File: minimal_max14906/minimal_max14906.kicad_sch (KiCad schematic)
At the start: 75 parts, among them J1 CLP-114-02-G-D-BE, J2 CLP-102-02-G-D-BE, J3 CLP-102-02-G-D-BE, J4 CLP-102-02-G-D-BE, J5 CLP-102-02-G-D-BE, J6 CLP-102-02-G-D-BE, J7 CLP-102-02-G-D-BE, Q1 SI7309DN-T1-E3, Q2 SI7309DN-T1-E3, Q3 SI7309DN-T1-E3, Q4 SI7309DN-T1-E3, U1 MAX14906ATM+

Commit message: Backup
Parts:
- added D10, D11, D12, D13: 40 V, diode_footprints:DO-214AB-2, symbol UNITED_DIODES_DATA_BASE:D_SMCJ40A-CA
- added J10, J11, J8, J9: TBP02R2-381-02BE, connector_footprints:TBP02R2-381-02BE, symbol UNITED_CONNECTORS_DATA_BASE:J_TBP02R2-381-02BE
- C1, C10, C12, C3, C4, C9: value 1 uF -> 1 µF; 3dviewer Link (none) -> https://3dviewer.net/index.html#model=https://github.com/io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; Capacitor Type (none) -> Ceramic
- C11, C2: value 0.1uF -> 100 nF; 3dviewer Link (none) -> https://3dviewer.net/index.html#model=https://github.com/io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; Capacitor Type (none) -> Ceramic
- C13: value 10 uF -> 10 µF; 3dviewer Link (none) -> https://3dviewer.net/index.html#model=https://github.com/io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; Capacitor Type (none) -> Ceramic
- C5, C6, C7, C8: 3dviewer Link (none) -> https://3dviewer.net/index.html#model=https://github.com/io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; Capacitor Type (none) -> Ceramic
- D1, D2, D4, D6, D8: value APHHS1005CGCK -> 1.8 V
- D3, D5, D7, D9: value APHHS1005LSECK/J3-PF -> 1.8 V
- J1, J2, J3, J4, J5, J6, J7: Mounting Style Through Hole -> Surface Mount
- Q1, Q2, Q3, Q4: value SI7309DN-T1-E3 -> -60.0 V; 3dviewer Link (none) -> https://3dviewer.net/index.html#model=https://github.com/io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
- R1: value 24.9k -> 24.9 kΩ; 3dviewer Link (none) -> https://3dviewer.net/index.html#model=https://github.com/io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; Component Type (none) -> Resistor
- R2, R3, R4, R5: value 5.6k -> 5.6 kΩ; 3dviewer Link (none) -> https://3dviewer.net/index.html#model=https://github.com/io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; Component Type (none) -> Resistor
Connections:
- net CHANNEL_1: now also D12.1, J10.2
- net CHANNEL_2: now also D13.1, J11.1
- net CHANNEL_3: now also D11.1, J9.2
- net CHANNEL_4: now also D10.1, J8.1
- net GNDA: now also D10.2, D11.2, D12.2, D13.2, J10.1, J11.2, J8.2, J9.1
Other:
- moved on the sheet: J4, TP15, TP16, TP17, TP18, TP20, TP21, TP22, TP23, TP24, TP25, TP26

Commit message: Switch to KiCad 9
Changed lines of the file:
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@@
 (kicad_sch
-	(version 20231120)
+	(version 20250114)
 	(generator "eeschema")
-	(generator_version "8.0")
+	(generator_version "9.0")
 	(paper "A3")
 	(junction
@@
 		)
 	)
+	(embedded_fonts no)
 )

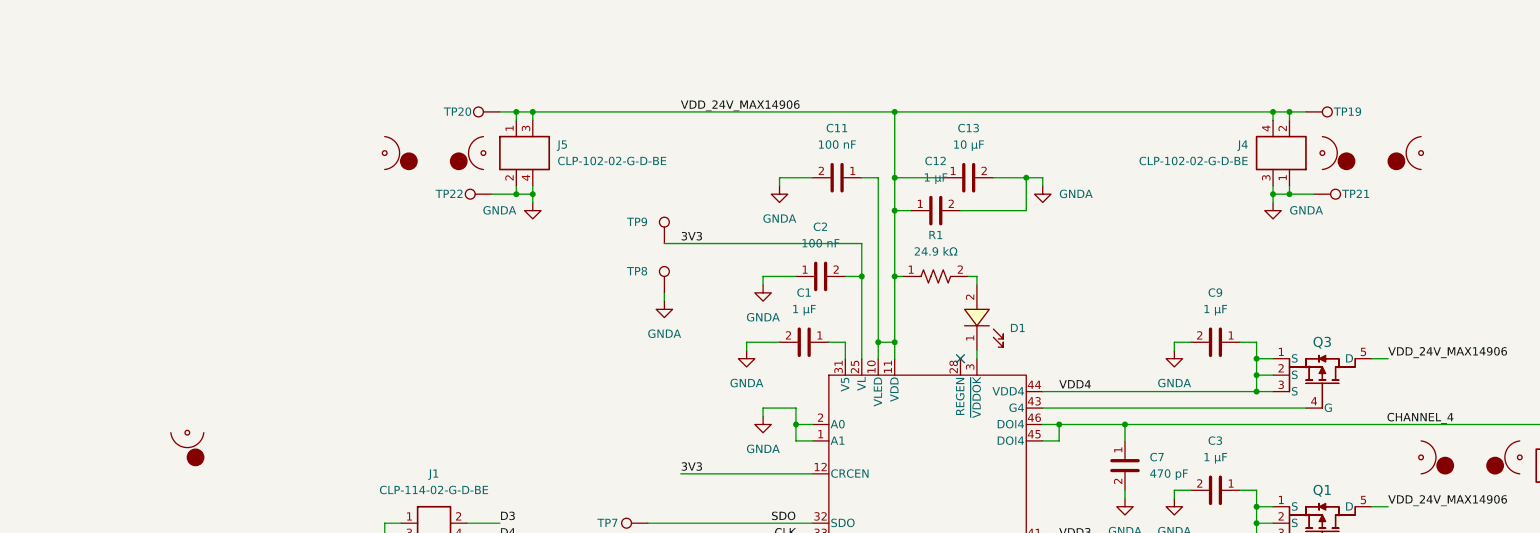
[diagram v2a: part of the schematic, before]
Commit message: Update pad dimensions and add net colors for minimal_max14906
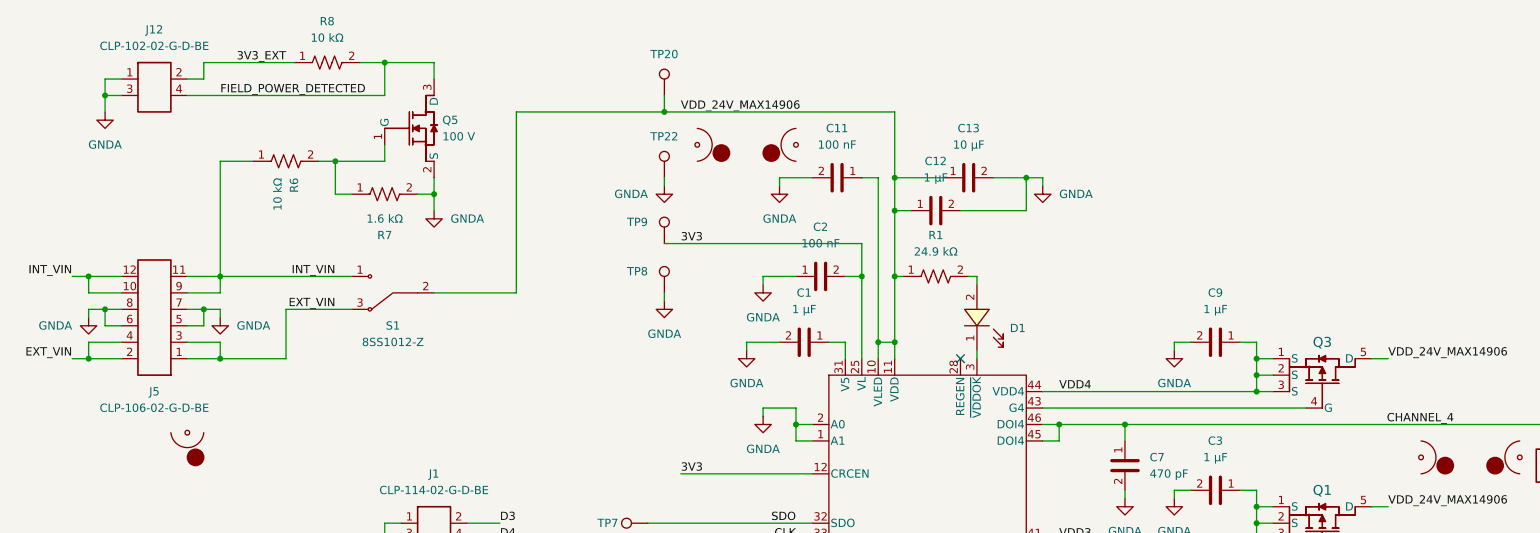
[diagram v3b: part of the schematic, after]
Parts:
- removed J4: CLP-102-02-G-D-BE, connector_footprints:CLP-102-02-G-D-BE, symbol UNITED_CONNECTORS_DATA_BASE:J_CLP-102-02-G-D-BE
- removed MB4: mouse-bite-midle-50mil-200mil, mouse_bite_footprints:mouse-bite-midle-50mil-200mil, symbol UNITED_MOUSE_BITES_DATA_BASE:mouse-bite-midle-50mil-200mil
- removed TP19, TP21: TestPoint, test_point_footprints:TestPoint_THTPad_Castelated, symbol UNITED_TEST_POINTS:TestPoint_Castelated
- added J12: CLP-102-02-G-D-BE, connector_footprints:CLP-102-02-G-D-BE, symbol UNITED_CONNECTORS_DATA_BASE:J_CLP-102-02-G-D-BE
- added Q5: 100 V, transistor_footprints:SOT-323, symbol UNITED_TRANSISTORS_DATA_BASE:Q_BSS123WQ-7-F
- added R6, R8: 10 kΩ, resistor_footprints:R_0402_1005Metric, symbol UNITED_RESISTORS_DATA_BASE:R_ERJ-2RKF1002X
- added R7: 1.6 kΩ, resistor_footprints:R_0402_1005Metric, symbol UNITED_RESISTORS_DATA_BASE:R_ERJ-2RKF1601X
- added S1: 8SS1012-Z, switches_footprints:8SS1012-Z, symbol UNITED_SWITCHES_DATA_BASE:S_8SS1012-Z
- J5: value CLP-102-02-G-D-BE -> CLP-106-02-G-D-BE; footprint connector_footprints:CLP-102-02-G-D-BE -> connector_footprints:CLP-106-02-G-D-BE; symbol UNITED_CONNECTORS_DATA_BASE:J_CLP-102-02-G-D-BE -> UNITED_CONNECTORS_DATA_BASE:J_CLP-106-02-G-D-BE; MPN CLP-102-02-G-D-BE -> CLP-106-02-G-D-BE; Pin Count 2 -> 6; Symbol Name J_CLP-102-02-G-D-BE -> J_CLP-106-02-G-D-BE; Trustedparts Search https://www.trustedparts.com/en/search/CLP-102-02-G-D-BE -> https://www.trustedparts.com/en/search/CLP-106-02-G-D-BE
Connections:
- net GNDA: now also J5.5, J5.6, J5.7, J5.8, J12.1, J12.3, Q5.2 (S), R7.2; no longer J5.2, J5.4
- net VDD_24V_MAX14906: now also S1.2; no longer J5.1, J5.3
- new net: Q5.1 (G), R6.2, R7.1
- new net 3V3_EXT: J12.2, R8.1
- new net EXT_VIN: J5.1, J5.2, J5.3, J5.4, S1.3
- new net FIELD_POWER_DETECTED: J12.4, Q5.3 (D), R8.2
- new net INT_VIN: J5.10, J5.11, J5.12, J5.9, R6.1, S1.1
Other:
- moved on the sheet: TP20, TP22

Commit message: backup
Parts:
- J5: value CLP-106-02-G-D-BE -> CLP-103-02-G-D-BE; footprint connector_footprints:CLP-106-02-G-D-BE -> connector_footprints:CLP-103-02-G-D-BE; symbol UNITED_CONNECTORS_DATA_BASE:J_CLP-106-02-G-D-BE -> UNITED_CONNECTORS_DATA_BASE:J_CLP-103-02-G-D-BE; MPN CLP-106-02-G-D-BE -> CLP-103-02-G-D-BE; Pin Count 6 -> 3; Symbol Name J_CLP-106-02-G-D-BE -> J_CLP-103-02-G-D-BE; Trustedparts Search https://www.trustedparts.com/en/search/CLP-106-02-G-D-BE -> https://www.trustedparts.com/en/search/CLP-103-02-G-D-BE
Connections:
- net EXT_VIN: now also J5.5, J5.6; no longer J5.1, J5.2, J5.3, J5.4
- net GNDA: now also J5.3, J5.4; no longer J5.5, J5.6, J5.7, J5.8
- net INT_VIN: now also J5.1, J5.2; no longer J5.10, J5.11, J5.12, J5.9

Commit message: development backup
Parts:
- added C1, C13, C14, C15, C16, C2, C3, C4: 100 nF, capacitor_footprints:C_0402_1005Metric, symbol UNITED_CAPACITORS_DATA_BASE:C_GCM155R71H104KE02D
- added C10, C11, C12, C5, C6, C7, C8, C9: 1 nF, capacitor_footprints:C_0402_1005Metric, symbol UNITED_CAPACITORS_DATA_BASE:C_GCM155R71H102KA37D
- added J6: CLP-102-02-G-D-BE, connector_footprints:CLP-102-02-G-D-BE, symbol UNITED_CONNECTORS_DATA_BASE:J_CLP-102-02-G-D-BE
- added U1, U4: ADUM1252AUA+, analog_devices_footprints:21-0036_ADI, symbol UNITED_IC_ADI:U_ADUM1252AUA+
- added U2: MAX22441CAEE+, analog_devices_footprints:21-0055_E16MS&plus_1F_ADI, symbol UNITED_IC_ADI:U_MAX22441CAEE+
- added U3: MAX22442CAEE+, analog_devices_footprints:21-0055_E16MS&plus_1F_ADI, symbol UNITED_IC_ADI:U_MAX22442CAEE+
- renumbered C1 to C17, C2 to C18, C3 to C19, C4 to C20, C5 to C21, C6 to C22, C7 to C23, C8 to C24, C9 to C25, C10 to C26, C11 to C27, C12 to C28, C13 to C29, D11 to D1, D8 to D10, D9 to D11, D10 to D12, D12 to D13, D13 to D2, D1 to D3, D2 to D4, D3 to D5, D4 to D6, D5 to D7, D6 to D8, D7 to D9, J8 to J10, J10 to J11, J5 to J12, J9 to J2, J11 to J3, J2 to J4, J3 to J5, J6 to J7, J7 to J8, J12 to J9, MB6 to MB4, MB7 to MB5, MB5 to MB6, R7 to R6, R6 to R7, TP9 to TP1, TP11 to TP10, TP3 to TP11, TP13 to TP12, TP14 to TP13, TP8 to TP14, TP23 to TP19, TP1 to TP2, TP24 to TP20, TP25 to TP21, TP26 to TP22, TP20 to TP23, TP22 to TP24, TP2 to TP3, TP7 to TP4, TP6 to TP5, TP4 to TP6, TP5 to TP7, TP12 to TP8, TP10 to TP9, U1 to U5
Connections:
- net 3V3: now also C10.1, C11.1, C12.1, C13.1, C14.1, C15.1, C16.1, C9.1, J6.1, J6.3, U1.8 (VDD2), U2.10 (ENB), U2.16 (VDDB), U3.10 (ENB), U3.16 (VDDB), U4.8 (VDD2); no longer J1.18, TP1.1
- net CHANNEL_1: now also J11.1; no longer J11.2
- net CHANNEL_3: now also J2.1; no longer J2.2
- net CLK: now also U2.13 (OUT2); no longer J1.12, TP5.1
- net D1: now also U4.6 (SCL2); no longer J1.26, TP12.1
- net D2: now also U4.7 (SDA2); no longer J1.28, TP13.1
- net D3: now also U1.6 (SCL2); no longer J1.2, TP2.1
- net D4: now also U1.7 (SDA2); no longer J1.4, TP3.1
- net EN: now also U3.13 (OUT2); no longer J1.22, TP10.1
- net GNDA: now also J11.2, J2.2, C10.2, C11.2, C12.2, C13.2, C14.2, C15.2, C16.2, C9.2, J6.2, J6.4, U1.5 (GND2), U2.15 (GNDB), U2.9 (GNDB), U3.15 (GNDB), U3.9 (GNDB), U4.5 (GND2); no longer J1.1, J1.11, J1.13, J1.15, J1.16, J1.17, J1.19, J1.21, J1.23, J1.25, J1.27, J1.3, J1.5, J1.7, J1.9, J11.1, J2.1, TP14.1
- net SDI: now also U2.14 (OUT1); no longer J1.8, TP6.1
- net SDO: now also U2.11 (IN4); no longer J1.14, TP4.1
- net SYNCH: now also U3.14 (OUT1); no longer J1.6, TP11.1
- net ~{CS}: now also U2.12 (OUT3); no longer J1.10, TP7.1
- net ~{FAULT}: now also U3.12 (IN3); no longer J1.20, TP9.1
- net ~{READY}: now also U3.11 (IN4); no longer J1.24, TP8.1
- new net 3V3_ISO: C1.1, C2.1, C3.1, C4.1, C5.1, C6.1, C7.1, C8.1, J1.14, TP1.1, U1.1 (VDD1), U2.1 (VDDA), U2.7 (ENA), U3.1 (VDDA), U3.7 (ENA), U4.1 (VDD1)
- new net CLK_ISO: J1.10, TP6.1, U2.4 (IN2)
- new net D1_ISO: J1.26, TP12.1, U4.3 (SCL1)
- new net D2_ISO: J1.28, TP13.1, U4.2 (SDA1)
- new net D3_ISO: J1.2, TP2.1, U1.3 (SCL1)
- new net D4_ISO: J1.4, TP3.1, U1.2 (SDA1)
- new net EN_ISO: J1.22, TP10.1, U3.4 (IN2)
- new net GND: C1.2, C2.2, C3.2, C4.2, C5.2, C6.2, C7.2, C8.2, J1.1, J1.11, J1.13, J1.15, J1.16, J1.17, J1.19, J1.21, J1.23, J1.25, J1.27, J1.3, J1.5, J1.7, J1.9, TP14.1, U1.4 (GND1), U2.2 (GNDA), U2.8 (GNDA), U3.2 (GNDA), U3.8 (GNDA), U4.4 (GND1)
- new net SDI_ISO: J1.12, TP7.1, U2.3 (IN1)
- new net SDO_ISO: J1.6, TP4.1, U2.6 (OUT4)
- new net SYNCH_ISO: J1.24, TP11.1, U3.3 (IN1)
- new net ~{CS_ISO}: J1.8, TP5.1, U2.5 (IN3)
- new net ~{FAULT_ISO}: J1.20, TP9.1, U3.5 (OUT3)
- new net ~{READY_ISO}: J1.18, TP8.1, U3.6 (OUT4)
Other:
- moved on the sheet: D10, D11, D4, D5, D6, D7, D8, D9, J1, J12, J9, Q5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

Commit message: development backup
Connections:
- net CHANNEL_1: now also J8.4; no longer J8.1
- net CHANNEL_2: now also J5.1; no longer J5.4
- net CHANNEL_3: now also J4.4; no longer J4.1
- net CHANNEL_4: now also J7.1; no longer J7.4
- net GNDA: now also J4.1, J5.4, J7.4, J8.1; no longer J4.4, J5.1, J7.1, J8.4
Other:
- moved on the sheet: J4, J5, J7, J8, TP15, TP16, TP17, TP18, TP19, TP20, TP21, TP22

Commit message: development backup
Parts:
- removed D1, D12, D13, D2: 40 V, diode_footprints:DO-214AB-2, symbol UNITED_DIODES_DATA_BASE:D_SMCJ40A-CA
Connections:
- net CHANNEL_1: now also J8.1, J8.2; no longer J8.3, J8.4
- net CHANNEL_3: now also J4.1, J4.2; no longer J4.3, J4.4
- net GNDA: now also J4.3, J4.4, J8.3, J8.4; no longer J4.1, J4.2, J8.1, J8.2
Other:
- moved on the sheet: J10, J11, J2, J3

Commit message: development backup
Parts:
- removed J1: CLP-114-02-G-D-BE, connector_footprints:CLP-114-02-G-D-BE, symbol UNITED_CONNECTORS_DATA_BASE:J_CLP-114-02-G-D-BE
- removed MB1: mouse-bite-midle-50mil-200mil, mouse_bite_footprints:mouse-bite-50mil-790mil, symbol UNITED_MOUSE_BITES_DATA_BASE:mouse-bite-50mil-790mil
- added J13, J14: CLP-108-02-G-D-BE, connector_footprints:CLP-108-02-G-D-BE, symbol UNITED_CONNECTORS_DATA_BASE:J_CLP-108-02-G-D-BE
- added TP25, TP26: TestPoint, test_point_footprints:TestPoint_THTPad_Castelated, symbol UNITED_TEST_POINTS:TestPoint_Castelated
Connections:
- net 3V3_ISO: now also J13.3, J14.13, TP25.1
- net CLK_ISO: now also J13.9
- net D1_ISO: now also J14.1
- net D2_ISO: now also J14.3
- net D3_ISO: now also J13.13
- net D4_ISO: now also J13.15
- net EN_ISO: now also J14.5
- net GND: now also J13.1, J13.10, J13.12, J13.14, J13.16, J13.2, J13.4, J13.6, J13.8, J14.10, J14.12, J14.14, J14.15, J14.16, J14.2, J14.4, J14.6, J14.8, TP26.1
- net SDI_ISO: now also J13.11
- net SDO_ISO: now also J13.7
- net SYNCH_ISO: now also J14.7
- net ~{CS_ISO}: now also J13.5
- net ~{FAULT_ISO}: now also J14.9
- net ~{READY_ISO}: now also J14.11
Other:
- moved on the sheet: TP1, TP10, TP11, TP12, TP13, TP14, TP2, TP3, TP4, TP5, TP6, TP7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
